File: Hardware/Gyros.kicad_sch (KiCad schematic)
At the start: 12 parts, among them U5 BHI160B, U6 BMM150

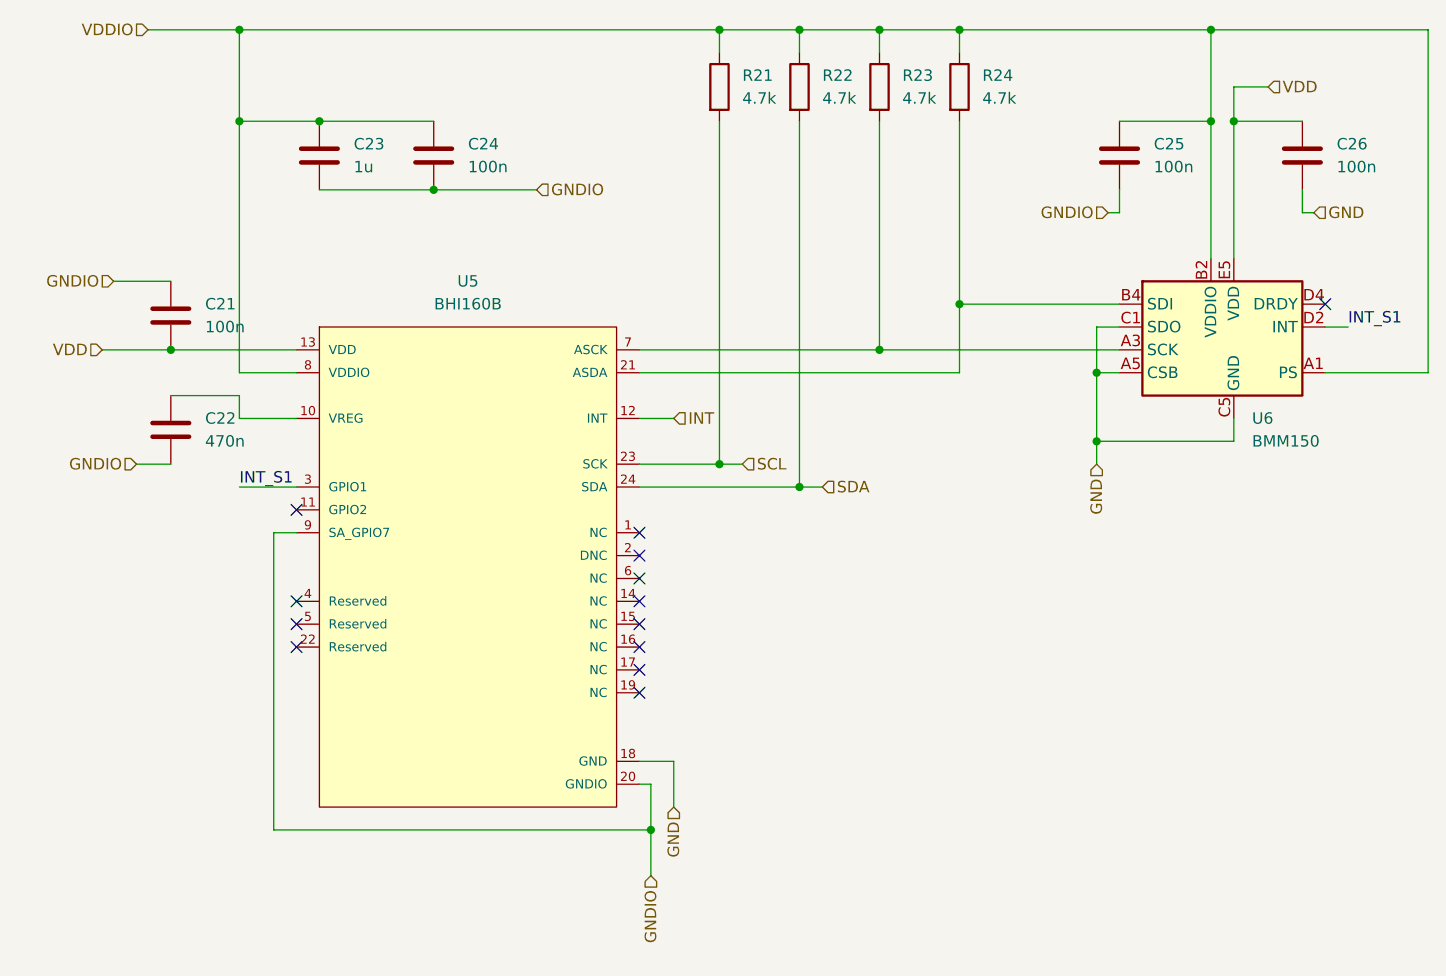
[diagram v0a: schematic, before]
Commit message: Inverted TX/RX from ESP32 - added INT line from BHI - Changed ESP32 dbg port to bigger footprint
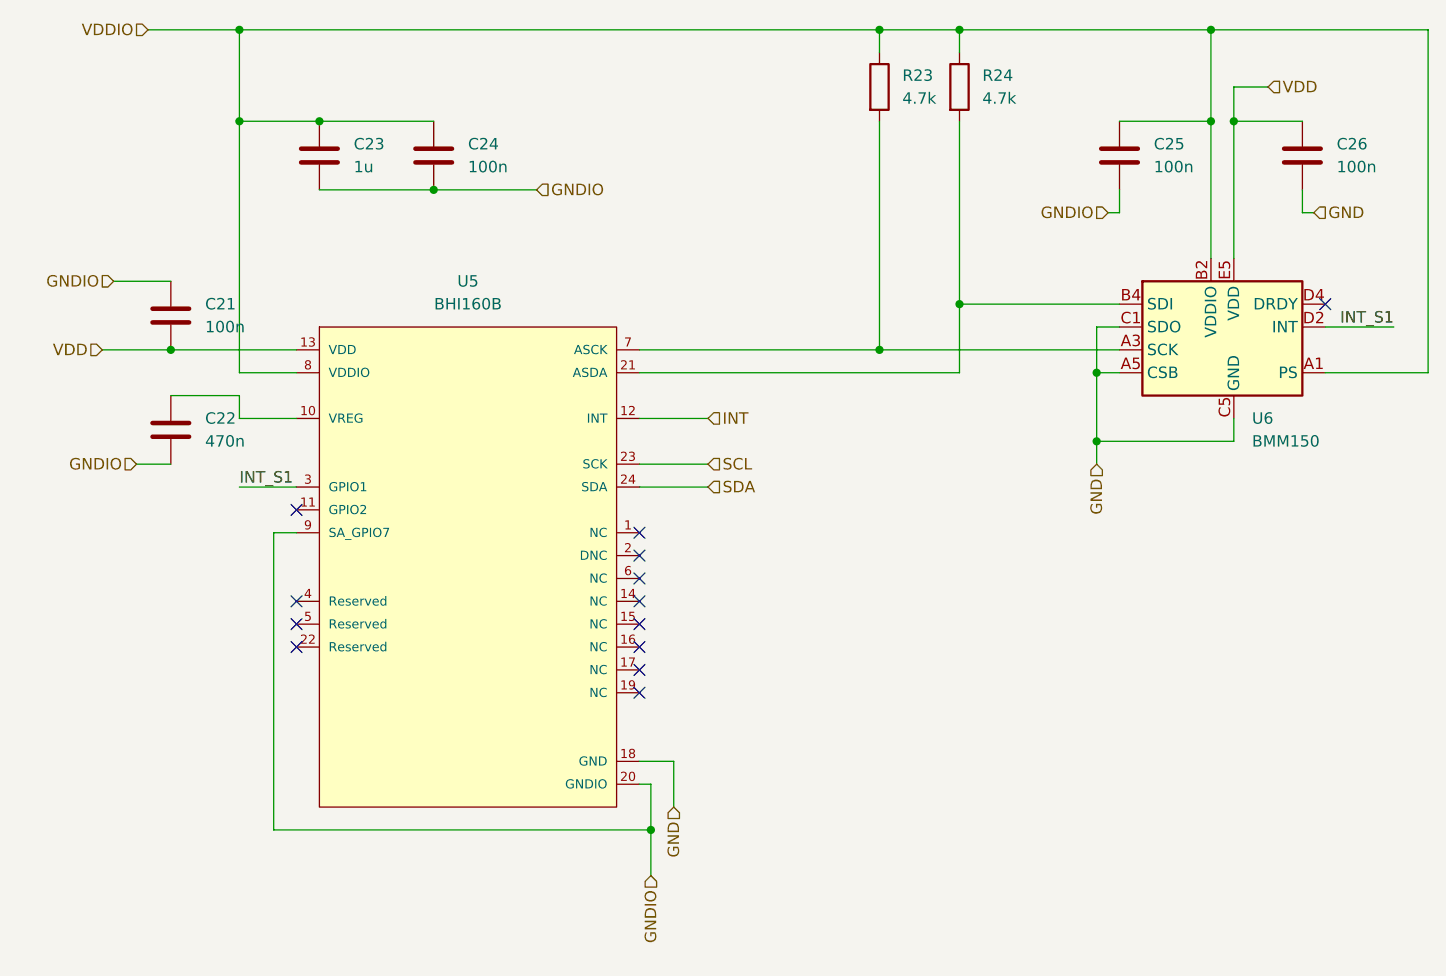
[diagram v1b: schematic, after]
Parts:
- removed R21, R22: 4.7k, Resistor_SMD:R_0402_1005Metric, symbol Device:R

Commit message: First modification for v2
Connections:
- net INT_SCK: now reaches R23.2, U5.7 (ASCK), U6.A3 (SCK)
- net INT_SDA: now reaches R24.2, U5.21 (ASDA), U6.B4 (SDI)
- net INT_S1 renamed INT_INT
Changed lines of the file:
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@@
   (junction (at 62.23 39.37) (diameter 0) (color 0 0 0 0)
   )
+  (junction (at 104.775 67.31) (diameter 0) (color 0 0 0 0)
+  )
   (junction (at 133.35 29.21) (diameter 0) (color 0 0 0 0)
   )
@@
   )
   (junction (at 148.59 67.31) (diameter 0) (color 0 0 0 0)
+  )
+  (junction (at 108.585 64.77) (diameter 0) (color 0 0 0 0)
   )
   (junction (at 133.35 59.69) (diameter 0) (color 0 0 0 0)
@@
     (stroke (width 0) (type default))
   )
+  (wire (pts (xy 39.37 80.01) (xy 59.69 80.01))
+    (stroke (width 0) (type default))
+  )
   (wire (pts (xy 57.15 118.11) (xy 57.15 85.09))
     (stroke (width 0) (type default))
   )
+  (wire (pts (xy 108.585 64.77) (xy 124.46 64.77))
+    (stroke (width 0) (type default))
+  )
   (wire (pts (xy 53.34 29.21) (xy 53.34 39.37))
     (stroke (width 0) (type default))
   )
+  (wire (pts (xy 104.775 67.31) (xy 133.35 67.31))
+    (stroke (width 0) (type default))
+  )
   (wire (pts (xy 133.35 29.21) (xy 161.29 29.21))
     (stroke (width 0) (type default))
@@
     (stroke (width 0) (type default))
   )
-  (wire (pts (xy 41.91 77.47) (xy 45.72 77.47))
+  (wire (pts (xy 39.37 77.47) (xy 45.72 77.47))
     (stroke (width 0) (type default))
   )
@@
     (stroke (width 0) (type default))
   )
+  (wire (pts (xy 97.79 67.31) (xy 104.775 67.31))
+    (stroke (width 0) (type default))
+  )
   (wire (pts (xy 97.79 72.39) (xy 105.41 72.39))
     (stroke (width 0) (type default))
@@
     (stroke (width 0) (type default))
   )
-  (wire (pts (xy 97.79 67.31) (xy 133.35 67.31))
-    (stroke (width 0) (type default))
-  )
   (wire (pts (xy 151.13 39.37) (xy 161.29 39.37))
     (stroke (width 0) (type default))
@@
     (stroke (width 0) (type default))
   )
-  (wire (pts (xy 97.79 64.77) (xy 124.46 64.77))
-    (stroke (width 0) (type default))
-  )
   (wire (pts (xy 148.59 67.31) (xy 148.59 74.93))
     (stroke (width 0) (type default))
@@
     (stroke (width 0) (type default))
   )
+  (wire (pts (xy 104.775 59.69) (xy 104.775 67.31))
+    (stroke (width 0) (type default))
+  )
   (wire (pts (xy 62.23 39.37) (xy 74.93 39.37))
     (stroke (width 0) (type default))
@@
     (stroke (width 0) (type default))
   )
-  (wire (pts (xy 38.1 64.77) (xy 45.72 64.77))
+  (wire (pts (xy 39.37 64.77) (xy 45.72 64.77))
     (stroke (width 0) (type default))
   )
@@
     (stroke (width 0) (type default))
   )
+  (wire (pts (xy 97.79 64.77) (xy 108.585 64.77))
+    (stroke (width 0) (type default))
+  )
   (wire (pts (xy 133.35 59.69) (xy 151.13 59.69))
     (stroke (width 0) (type default))
@@
     (stroke (width 0) (type default))
   )
-  (wire (pts (xy 53.34 80.01) (xy 59.69 80.01))
-    (stroke (width 0) (type default))
-  )
   (wire (pts (xy 161.29 29.21) (xy 161.29 39.37))
     (stroke (width 0) (type default))
@@
   )
   (wire (pts (xy 62.23 46.99) (xy 74.93 46.99))
+    (stroke (width 0) (type default))
+  )
+  (wire (pts (xy 108.585 59.69) (xy 108.585 64.77))
     (stroke (width 0) (type default))
   )
@@
     (effects (font (size 1.27 1.27)) (justify right bottom))
   )
-  (label "INT_S1" (at 53.34 80.01 0) (fields_autoplaced)
+  (label "INT_S1" (at 50.8 80.01 0) (fields_autoplaced)
     (effects (font (size 1.27 1.27)) (justify left bottom))
   )
-  (hierarchical_label "VDD" (shape input) (at 38.1 64.77 180) (fields_autoplaced)
+  (hierarchical_label "VDD" (shape input) (at 39.37 64.77 180) (fields_autoplaced)
     (effects (font (size 1.27 1.27)) (justify right))
   )
@@
     (effects (font (size 1.27 1.27)) (justify left))
   )
+  (hierarchical_label "INT_INT" (shape input) (at 39.37 80.01 180) (fields_autoplaced)
+    (effects (font (size 1.27 1.27)) (justify right))
+  )
   (hierarchical_label "GNDIO" (shape input) (at 149.86 49.53 180) (fields_autoplaced)
     (effects (font (size 1.27 1.27)) (justify right))
   )
+  (hierarchical_label "INT_SDA" (shape input) (at 104.775 59.69 90) (fields_autoplaced)
+    (effects (font (size 1.27 1.27)) (justify left))
+  )
   (hierarchical_label "INT" (shape input) (at 105.41 72.39 0) (fields_autoplaced)
     (effects (font (size 1.27 1.27)) (justify left))
@@
     (effects (font (size 1.27 1.27)) (justify right))
   )
-  (hierarchical_label "GNDIO" (shape input) (at 41.91 77.47 180) (fields_autoplaced)
+  (hierarchical_label "GNDIO" (shape input) (at 39.37 77.47 180) (fields_autoplaced)
     (effects (font (size 1.27 1.27)) (justify right))
   )
+  (hierarchical_label "INT_SCK" (shape input) (at 108.585 59.69 90) (fields_autoplaced)
+    (effects (font (size 1.27 1.27)) (justify left))
+  )
   (hierarchical_label "GND" (shape input) (at 101.6 115.57 270) (fields_autoplaced)
